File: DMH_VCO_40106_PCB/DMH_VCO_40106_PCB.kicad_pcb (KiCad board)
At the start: 2 copper layers, 98 x 135 mm, 147 parts, among them J10 Panel_GND, J100 IDC_02x08, J150 Conn_01x12, J300 AVR-ISP-6, Q1 BC558, Q2 BC548, Q3 BC548, Q4 BC548, Q5 BC548, Q6 BC548, Q7 J113, SW1 SW_SPDT_321_OnOff, SW2 SW_SPDT_321_OnOff, SW3 SW_SPDT_321_OnOff, U1 40106, U2 TL074, U3 TL074, U4 TL074, U5 ATtiny4313-P, U6 SM420561N

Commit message: Prepared PCBs for fabrication
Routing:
- net -12V: track 287.5 -> 286.1 mm
- net Net-(U5-PD6): track 58.3 -> 57.6 mm
- net +5V: track 153.3 -> 152.8 mm
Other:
- board text added: "Mk1.1 - September 2024"
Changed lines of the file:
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@@
 			(plot_on_all_layers_selection 0x0000000_00000000)
 			(disableapertmacros no)
-			(usegerberextensions no)
-			(usegerberattributes yes)
-			(usegerberadvancedattributes yes)
+			(usegerberextensions yes)
+			(usegerberattributes no)
+			(usegerberadvancedattributes no)
 			(creategerberjobfile yes)
 			(dashed_line_dash_ratio 12.000000)
@@
 			(plotinvisibletext no)
 			(sketchpadsonfab no)
-			(subtractmaskfromsilk no)
+			(subtractmaskfromsilk yes)
 			(outputformat 1)
 			(mirror no)
-			(drillshape 1)
+			(drillshape 0)
 			(scaleselection 1)
-			(outputdirectory "")
+			(outputdirectory "Gerbers/")
 		)
 	)
@@
 		)
 	)
+	(gr_text "Mk1.1 - September 2024"
+		(at 138.25 194.5 0)
+		(layer "B.SilkS")
+		(effects
+			(font
+				(size 1 1)
+				(thickness 0.25)
+				(bold yes)
+			)
+			(justify mirror)
+		)
+	)
 	(segment
 		(start 138.225 91.5)
@@
 	)
 	(segment
-		(start 80.25 74.5)
-		(end 91 74.5)
+		(start 110 177.25)
+		(end 110.799999 176.450001)
 		(width 1)
 		(layer "B.Cu")
@@
 	)
 	(segment
-		(start 110 177.25)
-		(end 110.799999 176.450001)
+		(start 91.044888 74.544888)
+		(end 91.044888 76)
 		(width 1)
 		(layer "B.Cu")
@@
 	)
 	(segment
-		(start 128.441816 133.5)
-		(end 132.53 133.5)
-		(width 1)
-		(layer "B.Cu")
-		(net 3)
-	)
-	(segment
-		(start 91.044888 74.544888)
-		(end 91.044888 76)
+		(start 90.25 73.75)
+		(end 91.044888 74.544888)
 		(width 1)
 		(layer "B.Cu")
@@
 	)
 	(segment
-		(start 106.94 180.31)
-		(end 110 177.25)
+		(start 134 135)
+		(end 134.03 135)
 		(width 1)
 		(layer "B.Cu")
@@
 	)
 	(segment
-		(start 110.799999 168.864999)
-		(end 108.68 166.745)
+		(start 94.08 76)
+		(end 91.044888 76)
 		(width 1)
 		(layer "B.Cu")
@@
 	)
 	(segment
-		(start 68.83 134.35)
-		(end 67.39 135.79)
+		(start 106.94 180.31)
+		(end 110 177.25)
 		(width 1)
 		(layer "B.Cu")
@@
 	)
 	(segment
-		(start 124.5 138.81)
-		(end 124.5 137.441816)
+		(start 110.799999 168.864999)
+		(end 108.68 166.745)
 		(width 1)
 		(layer "B.Cu")
@@
 	)
 	(segment
-		(start 78.5 82.44)
-		(end 77.19 83.75)
+		(start 68.83 134.35)
+		(end 67.39 135.79)
 		(width 1)
 		(layer "B.Cu")
@@
 	)
 	(segment
-		(start 95.5 74.58)
-		(end 92.464888 74.58)
+		(start 78.5 82.44)
+		(end 77.19 83.75)
 		(width 1)
 		(layer "B.Cu")
@@
 	)
 	(segment
-		(start 132.53 133.5)
-		(end 134.03 135)
+		(start 121.44 135.75)
+		(end 124.5 138.81)
 		(width 1)
 		(layer "B.Cu")
@@
 	)
 	(segment
-		(start 121.44 135.75)
-		(end 124.5 138.81)
+		(start 81 73.75)
+		(end 90.25 73.75)
 		(width 1)
 		(layer "B.Cu")
@@
 	)
 	(segment
-		(start 78.5 76.25)
-		(end 80.25 74.5)
+		(start 95.5 74.58)
+		(end 94.08 76)
 		(width 1)
 		(layer "B.Cu")
@@
 	)
 	(segment
-		(start 92.464888 74.58)
-		(end 91.044888 76)
+		(start 78.5 76.25)
+		(end 81 73.75)
 		(width 1)
 		(layer "B.Cu")
@@
 	)
 	(segment
-		(start 124.5 137.441816)
-		(end 128.441816 133.5)
+		(start 91.44 139)
+		(end 94.69 135.75)
 		(width 1)
 		(layer "B.Cu")
@@
 	)
 	(segment
-		(start 91 74.5)
-		(end 91.044888 74.544888)
+		(start 124.5 138.81)
+		(end 130.19 138.81)
 		(width 1)
 		(layer "B.Cu")
@@
 	)
 	(segment
-		(start 91.44 139)
-		(end 94.69 135.75)
+		(start 110.799999 176.450001)
+		(end 110.799999 168.864999)
 		(width 1)
 		(layer "B.Cu")
@@
 	)
 	(segment
-		(start 110.799999 176.450001)
-		(end 110.799999 168.864999)
+		(start 74.5 163.44)
+		(end 77.64 166.58)
 		(width 1)
 		(layer "B.Cu")
@@
 	)
 	(segment
-		(start 74.5 163.44)
-		(end 77.64 166.58)
+		(start 130.19 138.81)
+		(end 134 135)
 		(width 1)
 		(layer "B.Cu")
@@
 	)
 	(segment
-		(start 145.75 67.75)
-		(end 142.75 64.75)
+		(start 108 78)
+		(end 110.25 78)
 		(width 1)
 		(layer "F.Cu")
@@
 	)
 	(segment
-		(start 108 78)
-		(end 110.3 75.7)
+		(start 145.75 67.75)
+		(end 142.75 64.75)
 		(width 1)
 		(layer "F.Cu")
@@
 	)
 	(segment
-		(start 52.5 90.25)
-		(end 52.5 80.044888)
+		(start 110.3 77.95)
+		(end 110.3 67.8)
 		(width 1)
 		(layer "F.Cu")
@@
 	)
 	(segment
-		(start 110.3 75.7)
-		(end 110.3 67.8)
+		(start 52.5 90.25)
+		(end 52.5 80.044888)
 		(width 1)
 		(layer "F.Cu")
@@
 	)
 	(segment
+		(start 142.75 64.75)
+		(end 138.375 64.75)
+		(width 1)
+		(layer "F.Cu")
+		(net 4)
+	)
+	(segment
 		(start 110.3 67.8)
 		(end 108.96 66.46)
@@
 	)
 	(segment
-		(start 142.75 64.75)
-		(end 138.375 64.75)
+		(start 108.96 66.46)
+		(end 108.75 66.46)
 		(width 1)
 		(layer "F.Cu")
@@
 	)
 	(segment
-		(start 108.96 66.46)
-		(end 108.75 66.46)
+		(start 110.25 78)
+		(end 110.3 77.95)
 		(width 1)
 		(layer "F.Cu")
@@
 	)
 	(segment
-		(start 57.25 91.75)
-		(end 54 91.75)
-		(width 1)
-		(layer "B.Cu")
-		(net 4)
-	)
-	(segment
-		(start 62.75 86.25)
-		(end 57.25 91.75)
+		(start 101.68 81.07)
+		(end 101.68 81.01)
 		(width 1)
 		(layer "B.Cu")
@@
 	)
 	(segment
-		(start 96 90.19)
-		(end 97 89.19)
+		(start 104.99 81.01)
+		(end 108 78)
 		(width 1)
 		(layer "B.Cu")
@@
 	)
 	(segment
-		(start 104.99 81.01)
-		(end 108 78)
+		(start 62.25 86.75)
+		(end 57.25 91.75)
 		(width 1)
 		(layer "B.Cu")
@@
 	)
 	(segment
-		(start 96 90.19)
-		(end 92.06 86.25)
+		(start 96 86.75)
+		(end 62.25 86.75)
 		(width 1)
 		(layer "B.Cu")
@@
 	)
 	(segment
-		(start 92.06 86.25)
-		(end 62.75 86.25)
+		(start 96 86.75)
+		(end 101.68 81.07)
 		(width 1)
 		(layer "B.Cu")
@@
 	)
 	(segment
-		(start 97 85.69)
-		(end 101.68 81.01)
+		(start 96 90.19)
+		(end 96 86.75)
 		(width 1)
 		(layer "B.Cu")
@@
 	)
 	(segment
-		(start 97 89.19)
-		(end 97 85.69)
+		(start 57.25 91.75)
+		(end 54 91.75)
 		(width 1)
 		(layer "B.Cu")
@@
 	(segment
 		(start 101.203654 95.1)
-		(end 100.53 95.773654)
-		(width 0.3)
-		(layer "B.Cu")
-		(net 112)
-	)
-	(segment
-		(start 122.5 79.75)
-		(end 112.47 89.78)
-		(width 0.3)
-		(layer "B.Cu")
-		(net 112)
-	)
-	(segment
-		(start 131.25 65.5)
-		(end 130.25 66.5)
-		(width 0.3)
-		(layer "B.Cu")
-		(net 112)
-	)
-	(segment
-		(start 130.25 66.5)
-		(end 127.5 66.5)
+		(end 99.75 96.553654)
 		(width 0.3)
 		(layer "B.Cu")
@@
 	)
 	(segment
-		(start 102.156346 97.64)
-		(end 102.83 98.313654)
-		(width 0.3)
-		(layer "B.Cu")
-		(net 112)
-	)
-	(segment
 		(start 127.5 66.5)
 		(end 122.5 71.5)
@@
 	)
 	(segment
-		(start 122.5 71.5)
-		(end 122.5 79.75)
+		(start 112.47 89.78)
+		(end 108.97 89.78)
 		(width 0.3)
 		(layer "B.Cu")
@@
 	)
 	(segment
-		(start 112.47 89.78)
-		(end 108.97 89.78)
+		(start 131.25 65.5)
+		(end 130.25 66.5)
 		(width 0.3)
 		(layer "B.Cu")
@@
 	)
 	(segment
-		(start 102.83 102.72)
-		(end 101.68 103.87)
+		(start 103.65 95.1)
+		(end 101.203654 95.1)
 		(width 0.3)
 		(layer "B.Cu")
@@
 	)
 	(segment
-		(start 102.83 98.313654)
-		(end 102.83 102.72)
+		(start 122.5 71.5)
+		(end 122.5 79.75)
 		(width 0.3)
 		(layer "B.Cu")
@@
 	)
 	(segment
-		(start 101.443654 97.64)
-		(end 102.156346 97.64)
+		(start 122.5 79.75)
+		(end 112.47 89.78)
 		(width 0.3)
 		(layer "B.Cu")
@@
 	)
 	(segment
-		(start 103.65 95.1)
-		(end 101.203654 95.1)
+		(start 130.25 66.5)
+		(end 127.5 66.5)
 		(width 0.3)
 		(layer "B.Cu")
@@
 	)
 	(segment
-		(start 100.53 95.773654)
-		(end 100.53 96.726346)
+		(start 99.75 101.94)
+		(end 101.68 103.87)
 		(width 0.3)
 		(layer "B.Cu")
@@
 	)
 	(segment
-		(start 100.53 96.726346)
-		(end 101.443654 97.64)
+		(start 99.75 96.553654)
+		(end 99.75 101.94)
 		(width 0.3)
 		(layer "B.Cu")

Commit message: Replaced JLCJLCJLCJLC with space for serial number
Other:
- board text removed: "JLCJLCJLCJLC"
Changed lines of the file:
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@@
 		)
+	)
+	(gr_rect
+		(start 137.75 195)
+		(end 147.75 197)
+		(stroke
+			(width 0.1)
+			(type solid)
+		)
+		(fill solid)
+		(layer "B.SilkS")
 	)
 	(gr_circle
@@
 		(layer "User.9")
 	)
-	(gr_text "JLCJLCJLCJLC"
-		(at 142.75 196.25 0)
+	(gr_text "Mk1.1 - September 2024"
+		(at 138.25 193.75 0)
 		(layer "B.SilkS")
 		(effects
-			(font
-				(size 1 1)
-				(thickness 0.15)
-			)
-			(justify mirror)
-		)
-	)
-	(gr_text "Mk1.1 - September 2024"
-		(at 138.25 194.5 0)
-		(layer "B.SilkS")
-		(effects

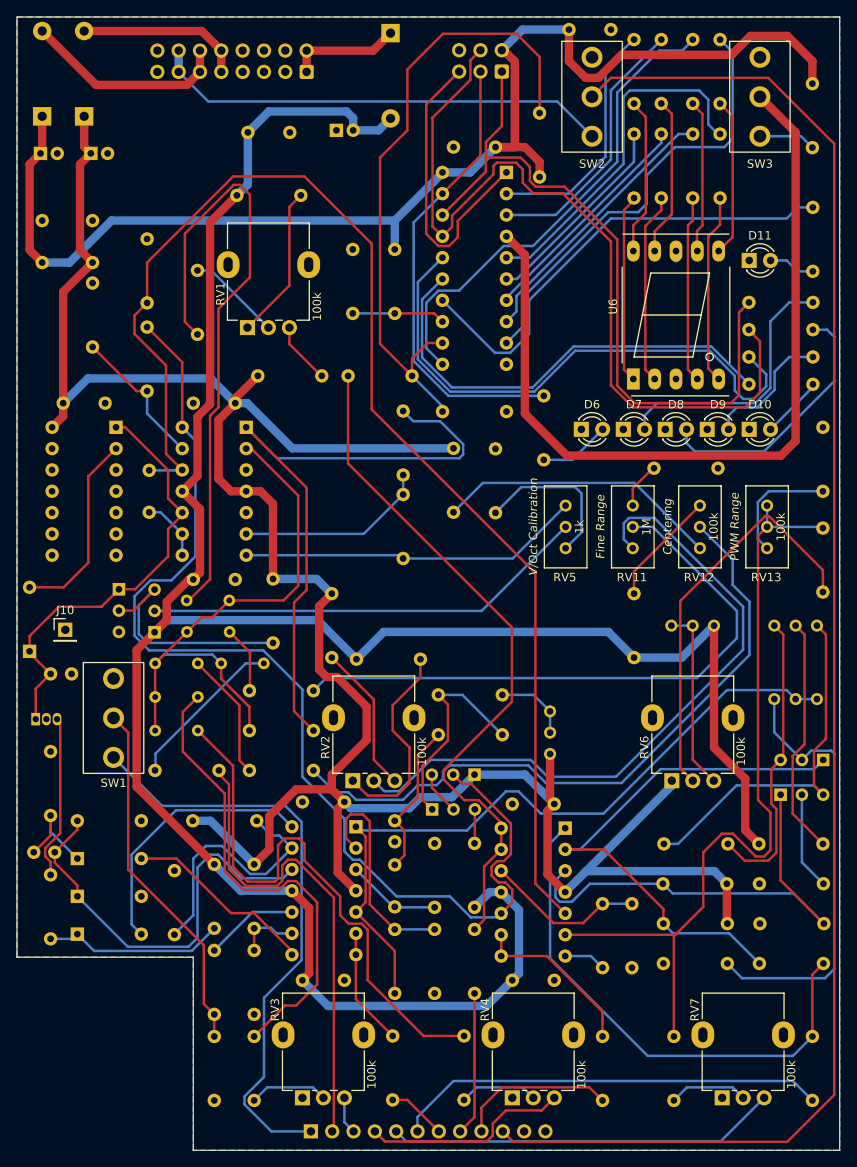
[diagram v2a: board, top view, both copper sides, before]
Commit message: Added 3D models to VCO
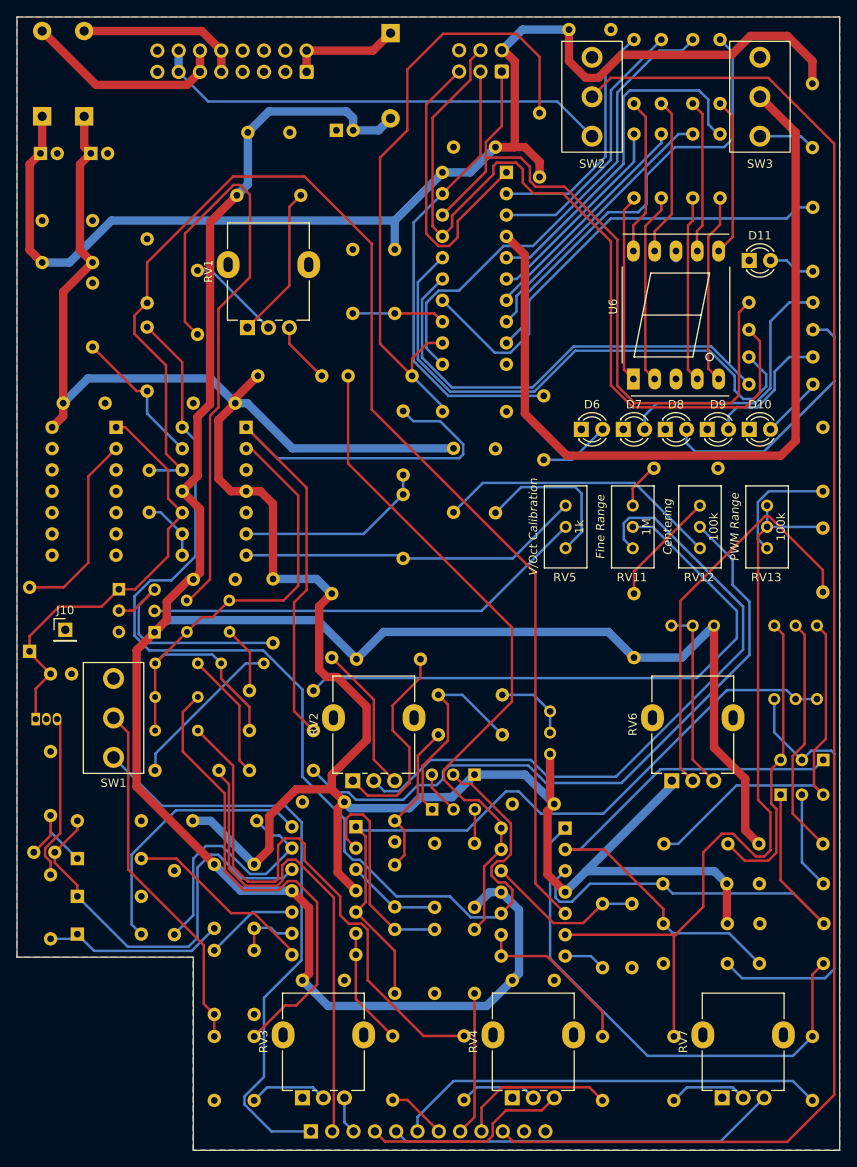
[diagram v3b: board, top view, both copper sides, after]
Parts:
- RV1, RV2, RV3, RV4, RV6, RV7: footprint Potentiometer_THT:Potentiometer_Alpha_RD901F-40-00D_Single_Vertical -> SynthStuff:Potentiometer_Alpha_RD901F-40-00D_Single_Vertical

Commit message: Added comments about deviations
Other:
- board text added: "Use 18k"
- board text added: "Use 1k"
- board text added: "silkscreen inverted"
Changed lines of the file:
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@@
+		(layer "Cmts.User")
+	)
+	(gr_poly
+		(pts
+			(xy 70.4 130.1) (xy 60.3 129.9) (xy 60.2 127.5) (xy 71 127.9) (xy 70.3 130.1) (xy 69.9 130.1)
+		)
+		(stroke
+			(width 0.1)
+			(type solid)
+		)
+		(fill none)
 		(layer "Cmts.User")
 	)
@@
 	)
 	(gr_circle
+		(center 146.3 115.7)
+		(end 146.2 118.2)
+		(stroke
+			(width 0.1)
+			(type default)
+		)
+		(fill none)
+		(layer "Cmts.User")
+	)
+	(gr_circle
 		(center 117.5 119.75)
 		(end 118.75 119.75)
@@
 			(type default)
 		)
+		(layer "Cmts.User")
+	)
+	(gr_circle
+		(center 80.070653 177.3)
+		(end 78.970653 179.4)
+		(stroke
+			(width 0.1)
+			(type default)
+		)
+		(fill none)
 		(layer "Cmts.User")
 	)
@@
 		)
 	)
+	(gr_text "Use 18k"
+		(at 76.8 176.5 0)
+		(layer "Cmts.User")
+		(effects
+			(font
+				(size 1 1)
+				(thickness 0.15)
+			)
+			(justify left bottom)
+		)
+	)
+	(gr_text "silkscreen inverted"
+		(at 59.3 127.1 0)
+		(layer "Cmts.User")
+		(effects
+			(font
+				(size 1 1)
+				(thickness 0.15)
+			)
+			(justify left bottom)
+		)
+	)
+	(gr_text "Use 1k"
+		(at 143.6 117.2 0)
+		(layer "Cmts.User")
+		(effects
+			(font
+				(size 1 1)
+				(thickness 0.15)
+			)
+			(justify left bottom)
+		)
+	)

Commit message: Fixed resistor values and regenerated gerbers
New gerbers version: Mk1.2
Includes fix with small font problem with the # sign under the blue LED on the front panel.
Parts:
- R5: value 10k -> 1k
- R59: value 20k -> 18k
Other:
- board text added: "Mk1.2 - October 2024"
- board text removed: "Mk1.1 - September 2024"
- board text removed: "Use 18k"
- board text removed: "Use 1k"
- board text removed: "silkscreen inverted"
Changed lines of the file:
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@@
 		)
 		(property "Value" "BC548"
-			(at -1.67 -4.86 180)
+			(at -1.67 0.64 180)
 			(layer "B.SilkS")
 			(effects
@@
 			)
 		)
-		(property "Value" "20k"
+		(property "Value" "18k"
 			(at 3.81 0 90)
 			(layer "B.SilkS")
@@
 			)
 		)
+		(property "Function" ""
+			(at 0 0 -90)
+			(unlocked yes)
+			(layer "B.Fab")
+			(hide yes)
+			(effects
+				(font
+					(size 1 1)
+					(thickness 0.15)
+				)
+				(justify mirror)
+			)
+		)
 		(property ki_fp_filters "R_*")
 		(sheetname "Core")
@@
 			)
 		)
-		(property "Value" "10k"
+		(property "Value" "1k"
 			(at 3.81 0 90)
 			(layer "B.SilkS")
@@
 		)
 		(property "Value" "BC558"
-			(at 6.79 -4.64 180)
+			(at 6.79 0.61 180)
 			(layer "B.SilkS")
 			(effects
@@
 		(layer "Cmts.User")
 	)
-	(gr_poly
-		(pts
-			(xy 70.4 130.1) (xy 60.3 129.9) (xy 60.2 127.5) (xy 71 127.9) (xy 70.3 130.1) (xy 69.9 130.1)
-		)
-		(stroke
-			(width 0.1)
-			(type solid)
-		)
-		(fill none)
-		(layer "Cmts.User")
-	)
 	(gr_circle
 		(center 124.5 111.62)
@@
 	)
 	(gr_circle
-		(center 146.3 115.7)
-		(end 146.2 118.2)
-		(stroke
-			(width 0.1)
-			(type default)
-		)
-		(fill none)
-		(layer "Cmts.User")
-	)
-	(gr_circle
 		(center 117.5 119.75)
 		(end 118.75 119.75)
@@
 	)
 	(gr_circle
-		(center 80.070653 177.3)
-		(end 78.970653 179.4)
-		(stroke
-			(width 0.1)
-			(type default)
-		)
-		(fill none)
-		(layer "Cmts.User")
-	)
-	(gr_circle
 		(center 149 62.5)
 		(end 149 63)
@@
 		(layer "User.9")
 	)
-	(gr_text "Mk1.1 - September 2024"
+	(gr_text "Mk1.2 - October 2024"
 		(at 138.25 193.75 0)
 		(layer "B.SilkS")
@@
 		)
 	)
-	(gr_text "Use 18k"
-		(at 76.8 176.5 0)
-		(layer "Cmts.User")
-		(effects
-			(font
-				(size 1 1)
-				(thickness 0.15)
-			)
-			(justify left bottom)
-		)
-	)
-	(gr_text "silkscreen inverted"
-		(at 59.3 127.1 0)
-		(layer "Cmts.User")
-		(effects
-			(font
-				(size 1 1)
-				(thickness 0.15)
-			)
-			(justify left bottom)
-		)
-	)
-	(gr_text "Use 1k"
-		(at 143.6 117.2 0)
-		(layer "Cmts.User")
-		(effects
-			(font
-				(size 1 1)
-				(thickness 0.15)
-			)
-			(justify left bottom)
-		)
-	)
